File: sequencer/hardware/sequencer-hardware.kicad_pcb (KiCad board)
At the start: 4 copper layers, 54 parts, among them J10 Conn_01x03, J11 Conn_01x05_Male, J12 Conn_01x05_Male, J13 Conn_01x03, J14 Conn_01x03, J15 Conn_01x05_Male, J16 Conn_01x05_Male, J17 Conn_01x03, J2 40Pin 0.1", J3 USB_B_Micro, J4 Conn_01x02_Male, J7 Conn_01x03_Male, J8 Conn_01x03_Male, J9 Conn_01x03, U4 NCP1117-3.3_TO252, U6 W25Q128JVS, U7 RP2040, Y1 12MHz 18pF

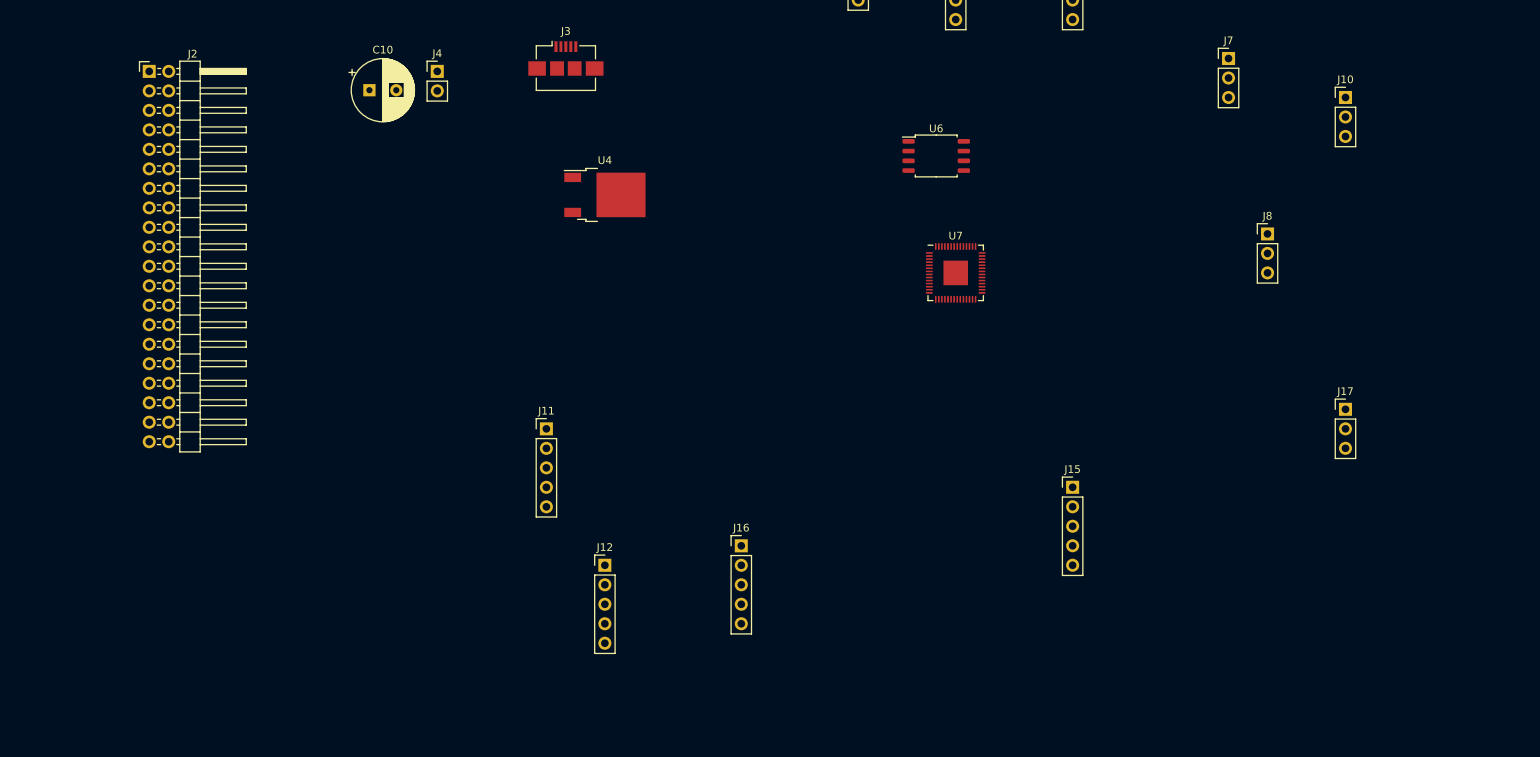
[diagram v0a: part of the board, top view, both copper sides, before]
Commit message: Disconnect GNDD from GNDA to prevent routing confusion
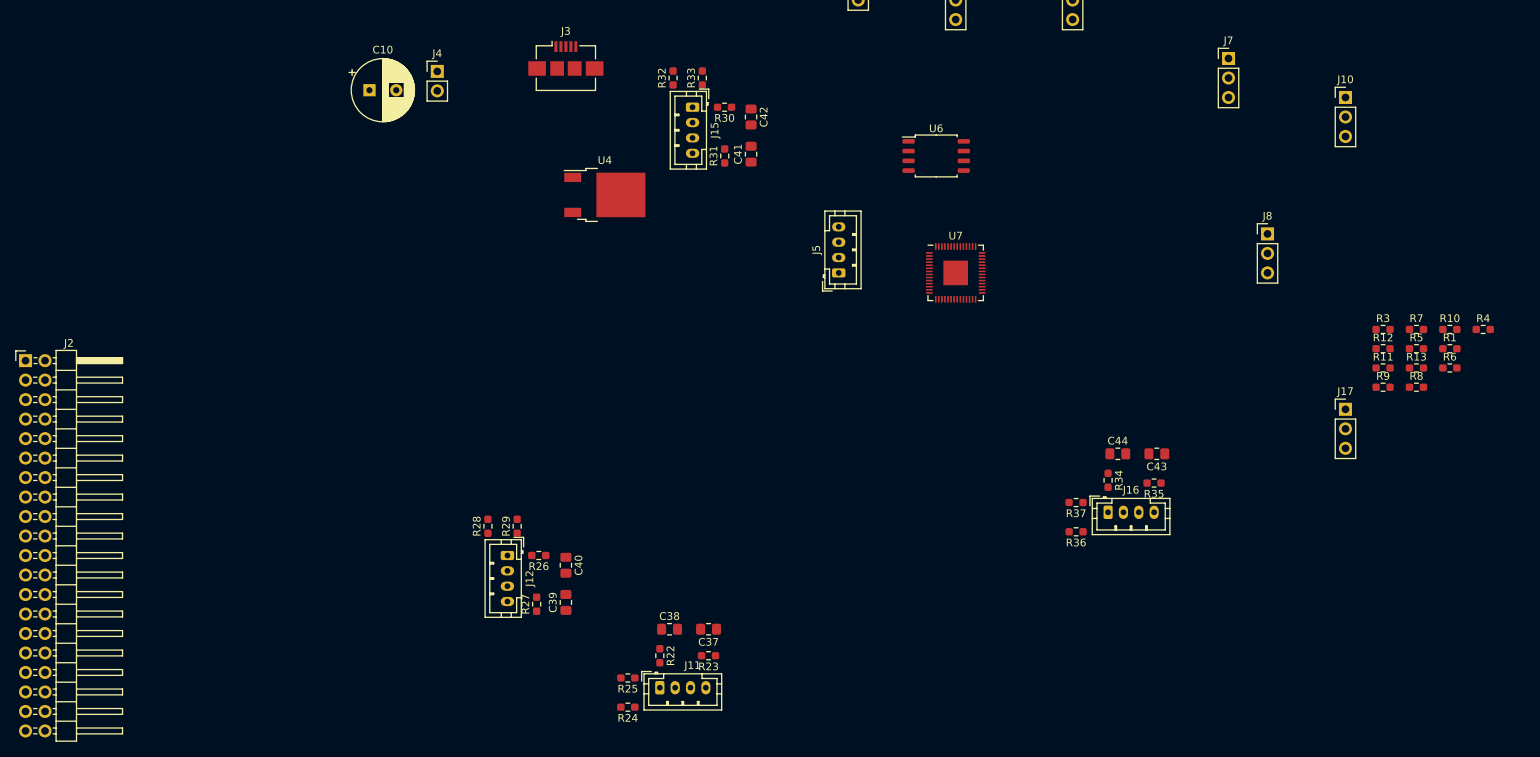
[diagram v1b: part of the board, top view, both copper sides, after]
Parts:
- added C37: 0.01u, Capacitor_SMD:C_0805_2012Metric_Pad1.18x1.45mm_HandSolder, F.Cu at (173.5, 130.3)
- added C38: 0.01u, Capacitor_SMD:C_0805_2012Metric_Pad1.18x1.45mm_HandSolder, F.Cu at (168.4, 130.3)
- added C39: 0.01u, Capacitor_SMD:C_0805_2012Metric_Pad1.18x1.45mm_HandSolder, F.Cu at (154.9, 126.8)
- added C40: 0.01u, Capacitor_SMD:C_0805_2012Metric_Pad1.18x1.45mm_HandSolder, F.Cu at (154.9, 121.9)
- added C41: 0.01u, Capacitor_SMD:C_0805_2012Metric_Pad1.18x1.45mm_HandSolder, F.Cu at (179.1, 68.3)
- added C42: 0.01u, Capacitor_SMD:C_0805_2012Metric_Pad1.18x1.45mm_HandSolder, F.Cu at (179.1, 63.5)
- added C43: 0.01u, Capacitor_SMD:C_0805_2012Metric_Pad1.18x1.45mm_HandSolder, F.Cu at (231.9, 107.4)
- added C44: 0.01u, Capacitor_SMD:C_0805_2012Metric_Pad1.18x1.45mm_HandSolder, F.Cu at (226.9, 107.4)
- added J5: JST 4-Pin male, Connector_JST:JST_PH_B4B-PH-K_1x04_P2.00mm_Vertical, F.Cu at (190.5, 83.8)
- added R1: 10k, Resistor_SMD:R_0603_1608Metric_Pad0.98x0.95mm_HandSolder, F.Cu at (270.1, 93.7)
- added R10: 10k, Resistor_SMD:R_0603_1608Metric_Pad0.98x0.95mm_HandSolder, F.Cu at (270.1, 91.2)
- added R11: 10k, Resistor_SMD:R_0603_1608Metric_Pad0.98x0.95mm_HandSolder, F.Cu at (261.4, 96.2)
- added R12: 10k, Resistor_SMD:R_0603_1608Metric_Pad0.98x0.95mm_HandSolder, F.Cu at (261.4, 93.7)
- added R13: 10k, Resistor_SMD:R_0603_1608Metric_Pad0.98x0.95mm_HandSolder, F.Cu at (265.8, 96.2)
- added R22: 10k, Resistor_SMD:R_0603_1608Metric_Pad0.98x0.95mm_HandSolder, F.Cu at (167.2, 133.7)
- added R23: 10k, Resistor_SMD:R_0603_1608Metric_Pad0.98x0.95mm_HandSolder, F.Cu at (173.5, 133.7)
- added R24: 10k, Resistor_SMD:R_0603_1608Metric_Pad0.98x0.95mm_HandSolder, F.Cu at (163.0, 140.4)
- added R25: 10k, Resistor_SMD:R_0603_1608Metric_Pad0.98x0.95mm_HandSolder, F.Cu at (163.0, 136.6)
- added R26: 10k, Resistor_SMD:R_0603_1608Metric_Pad0.98x0.95mm_HandSolder, F.Cu at (151.4, 120.7)
- added R27: 10k, Resistor_SMD:R_0603_1608Metric_Pad0.98x0.95mm_HandSolder, F.Cu at (151.1, 127.0)
- added R28: 10k, Resistor_SMD:R_0603_1608Metric_Pad0.98x0.95mm_HandSolder, F.Cu at (144.8, 116.8)
- added R29: 10k, Resistor_SMD:R_0603_1608Metric_Pad0.98x0.95mm_HandSolder, F.Cu at (148.6, 116.8)
- added R3: 10k, Resistor_SMD:R_0603_1608Metric_Pad0.98x0.95mm_HandSolder, F.Cu at (261.4, 91.2)
- added R30: 10k, Resistor_SMD:R_0603_1608Metric_Pad0.98x0.95mm_HandSolder, F.Cu at (175.6, 62.2)
- added R31: 10k, Resistor_SMD:R_0603_1608Metric_Pad0.98x0.95mm_HandSolder, F.Cu at (175.6, 68.6)
- added R32: 10k, Resistor_SMD:R_0603_1608Metric_Pad0.98x0.95mm_HandSolder, F.Cu at (168.9, 58.4)
- added R33: 10k, Resistor_SMD:R_0603_1608Metric_Pad0.98x0.95mm_HandSolder, F.Cu at (172.7, 58.4)
- added R34: 10k, Resistor_SMD:R_0603_1608Metric_Pad0.98x0.95mm_HandSolder, F.Cu at (225.6, 110.9)
- added R35: 10k, Resistor_SMD:R_0603_1608Metric_Pad0.98x0.95mm_HandSolder, F.Cu at (231.6, 111.2)
- added R36: 10k, Resistor_SMD:R_0603_1608Metric_Pad0.98x0.95mm_HandSolder, F.Cu at (221.4, 117.6)
- added R37: 10k, Resistor_SMD:R_0603_1608Metric_Pad0.98x0.95mm_HandSolder, F.Cu at (221.4, 113.8)
- added R4: 10k, Resistor_SMD:R_0603_1608Metric_Pad0.98x0.95mm_HandSolder, F.Cu at (274.5, 91.2)
- added R5: 10k, Resistor_SMD:R_0603_1608Metric_Pad0.98x0.95mm_HandSolder, F.Cu at (265.8, 93.7)
- added R6: 10k, Resistor_SMD:R_0603_1608Metric_Pad0.98x0.95mm_HandSolder, F.Cu at (270.1, 96.2)
- added R7: 10k, Resistor_SMD:R_0603_1608Metric_Pad0.98x0.95mm_HandSolder, F.Cu at (265.8, 91.2)
- added R8: 10k, Resistor_SMD:R_0603_1608Metric_Pad0.98x0.95mm_HandSolder, F.Cu at (265.8, 98.7)
- added R9: 10k, Resistor_SMD:R_0603_1608Metric_Pad0.98x0.95mm_HandSolder, F.Cu at (261.4, 98.7)
- J11, J12, J15, J16: value Conn_01x05_Male -> JST_4-pin_male; footprint Connector_PinHeader_2.54mm:PinHeader_1x05_P2.54mm_Vertical -> Connector_JST:JST_PH_B4B-PH-K_1x04_P2.00mm_Vertical
- moved J15 70.0 mm to (171.4, 62.2), turned to -90 degrees
- moved J16 48.0 mm to (225.6, 115.0)
- moved J2 41.0 mm to (84.5, 95.3)
- moved J11 36.8 mm to (167.2, 137.9)
- moved J12 12.8 mm to (147.3, 120.7), turned to -90 degrees
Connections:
- C10 pad 2: GNDA -> GNDD
- C11 pad 2: GNDA -> GNDD
- C20 pad 2: GNDA -> GNDD
- C21 pad 2: GNDA -> GNDD
- C22 pad 2: GNDA -> GNDD
- C23 pad 2: GNDA -> GNDD
- C24 pad 2: GNDA -> GNDD
- C25 pad 1: GNDA -> GNDD
- C26 pad 2: GNDA -> GNDD
- C27 pad 2: GNDA -> GNDD
- C28 pad 2: GNDA -> GNDD
- C29 pad 2: GNDA -> GNDD
- C30 pad 2: GNDA -> GNDD
- C31 pad 2: GNDA -> GNDD
- C32 pad 2: GNDA -> GNDD
- C33 pad 2: GNDA -> GNDD
- C34 pad 2: GNDA -> GNDD
- C35 pad 2: GNDA -> GNDD
- C36 pad 2: GNDA -> GNDD
- C9 pad 2: GNDA -> GNDD
- J10 pad 1: GNDA -> GNDD
- J11 pad 1: GNDA -> Net-(J11-Pad1)
- J11 pad 2: /D.R.U.M. Sequencer Digital/GPIO3_ENC02 -> GNDD
- J11 pad 3: /D.R.U.M. Sequencer Digital/GPIO2_ENC01 -> Net-(J11-Pad3)
- J11 pad 4: /D.R.U.M. Sequencer Digital/GPIO1_ENC00 -> unconnected-(J11-Pad4)
- J12 pad 1: GNDA -> Net-(J12-Pad1)
- J12 pad 2: /D.R.U.M. Sequencer Digital/GPIO11_ENC22 -> GNDD
- J12 pad 3: /D.R.U.M. Sequencer Digital/GPIO10_ENC21 -> Net-(J12-Pad3)
- J12 pad 4: /D.R.U.M. Sequencer Digital/GPIO9_ENC20 -> unconnected-(J12-Pad4)
- J13 pad 1: GNDA -> GNDD
- J14 pad 1: GNDA -> GNDD
- J15 pad 1: GNDA -> Net-(J15-Pad1)
- J15 pad 2: /D.R.U.M. Sequencer Digital/GPIO8_ENC12 -> GNDD
- J15 pad 3: /D.R.U.M. Sequencer Digital/GPIO7_ENC11 -> Net-(J15-Pad3)
- J15 pad 4: /D.R.U.M. Sequencer Digital/GPIO6_ENC10 -> unconnected-(J15-Pad4)
- J16 pad 1: GNDA -> Net-(J16-Pad1)
- J16 pad 2: /D.R.U.M. Sequencer Digital/GPIO14_ENC32 -> GNDD
- J16 pad 3: /D.R.U.M. Sequencer Digital/GPIO13_ENC31 -> Net-(J16-Pad3)
- J16 pad 4: /D.R.U.M. Sequencer Digital/GPIO12_ENC30 -> unconnected-(J16-Pad4)
- J17 pad 2: GNDA -> GNDD
- J2 pad 22: GNDA -> GNDD
- J2 pad 23: GNDA -> GNDD
- J2 pad 26: GNDA -> GNDD
- J2 pad 27: GNDA -> GNDD
- J2 pad 30: GNDA -> GNDD
- J2 pad 31: GNDA -> GNDD
- J2 pad 34: GNDA -> GNDD
- J2 pad 35: GNDA -> GNDD
- J2 pad 38: GNDA -> GNDD
- J2 pad 39: GNDA -> GNDD
- J3 pad 5: GNDA -> GNDD
- J3 pad 6: GNDA -> GNDD
- J7 pad 1: GNDA -> GNDD
- J8 pad 1: GNDA -> GNDD
- J9 pad 1: GNDA -> GNDD
- U4 pad 1: GNDA -> GNDD
- U6 pad 4: GNDA -> GNDD
- U7 pad 11: /D.R.U.M. Sequencer Digital/GPIO8_ENC12 -> unconnected-(U7-Pad11)
- U7 pad 14: /D.R.U.M. Sequencer Digital/GPIO11_ENC22 -> unconnected-(U7-Pad14)
- U7 pad 17: /D.R.U.M. Sequencer Digital/GPIO14_ENC32 -> unconnected-(U7-Pad17)
- U7 pad 19: GNDA -> GNDD
- U7 pad 5: /D.R.U.M. Sequencer Digital/GPIO3_ENC02 -> unconnected-(U7-Pad5)
- U7 pad 57: GNDA -> GNDD

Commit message: Do a lot of random stuff
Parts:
- added SW2: SW_Push, custom:TE_ConnMSLPT5252CG1, F.Cu at (212.1, 135.9)
- added SW3: SW_Push, custom:TE_ConnMSLPT5252CG1, F.Cu at (228.8, 135.9)
- added U5: OPA703UA, Package_SO:SOIC-8_3.9x4.9mm_P1.27mm, F.Cu at (59.9, 78.6)
- C21, C23, C29: value 1u -> 0.01u; footprint Capacitor_SMD:C_0603_1608Metric_Pad1.08x0.95mm_HandSolder -> Capacitor_SMD:C_0805_2012Metric_Pad1.18x1.45mm_HandSolder
- C24: value 0.1u -> 1u
- C25: value 27p -> 0.01u; footprint Capacitor_SMD:C_0603_1608Metric_Pad1.08x0.95mm_HandSolder -> Capacitor_SMD:C_0805_2012Metric_Pad1.18x1.45mm_HandSolder
- C26: value 27p -> 1u
- C27, C28, C30, C31: value 0.1u -> 0.01u; footprint Capacitor_SMD:C_0603_1608Metric_Pad1.08x0.95mm_HandSolder -> Capacitor_SMD:C_0805_2012Metric_Pad1.18x1.45mm_HandSolder
- C33, C34: value 0.1u -> 27p
- C36: value 1u -> 0.1u
- C37, C44: value 0.01u -> 1u; footprint Capacitor_SMD:C_0805_2012Metric_Pad1.18x1.45mm_HandSolder -> Capacitor_SMD:C_0603_1608Metric_Pad1.08x0.95mm_HandSolder
- C38, C39, C40, C41, C42, C43: value 0.01u -> 0.1u; footprint Capacitor_SMD:C_0805_2012Metric_Pad1.18x1.45mm_HandSolder -> Capacitor_SMD:C_0603_1608Metric_Pad1.08x0.95mm_HandSolder
- J10, J9: value Conn_01x03 -> JST_4-pin_male; footprint Connector_PinHeader_2.54mm:PinHeader_1x03_P2.54mm_Vertical -> Connector_JST:JST_PH_B4B-PH-K_1x04_P2.00mm_Vertical
- J11, J12: value JST_4-pin_male -> Conn_01x03; footprint Connector_JST:JST_PH_B4B-PH-K_1x04_P2.00mm_Vertical -> Connector_PinHeader_2.54mm:PinHeader_1x03_P2.54mm_Vertical
- R18, R21: value 1k -> 10k
- R19, R20: value 27 -> 10k
- R26, R37: value 10k -> 1k
- R35, R36: value 10k -> 27
- U6: value W25Q128JVS -> OPA703UA; footprint Package_SO:SOIC-8_5.23x5.23mm_P1.27mm -> Package_SO:SOIC-8_3.9x4.9mm_P1.27mm
- U7: value RP2040 -> W25Q128JVS; footprint Package_DFN_QFN:QFN-56-1EP_7x7mm_P0.4mm_EP3.2x3.2mm -> Package_SO:SOIC-8_5.23x5.23mm_P1.27mm
- moved R13 217.6 mm to (48.8, 80.9), turned to 180 degrees
- moved R4 209.8 mm to (65.5, 72.9), turned to 180 degrees
- moved R12 207.7 mm to (54.4, 78.0), turned to 180 degrees
- moved R6 205.4 mm to (65.5, 78.0), turned to 180 degrees
- moved R10 204.6 mm to (65.5, 88.1), turned to 180 degrees
- moved R11 202.1 mm to (59.8, 82.0), turned to 180 degrees
- moved R5 201.1 mm to (65.5, 75.4), turned to 180 degrees
- moved R8 200.9 mm to (65.5, 83.1), turned to 180 degrees
- moved R7 200.5 mm to (65.5, 80.5), turned to 180 degrees
- moved R3 197.0 mm to (65.5, 70.4), turned to 180 degrees
- moved R9 196.3 mm to (65.5, 85.6), turned to 180 degrees
- moved U6 154.7 mm to (48.8, 77.3), turned to 180 degrees
- moved C19 126.4 mm to (70.6, 88.1), turned to 180 degrees
- moved C18 118.6 mm to (70.6, 83.1)
- moved J10 117.6 mm to (167.6, 137.9)
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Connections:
- C21 pad 1: +3V3 -> /D.R.U.M. Sequencer Digital/GPIO2_ENC01
- C23 pad 1: +3V3 -> /D.R.U.M. Sequencer Digital/GPIO1_ENC00
- C25 pad 1: GNDD -> /D.R.U.M. Sequencer Digital/GPIO10_ENC21
- C25 pad 2: Net-(C25-Pad2) -> GNDD
- C26 pad 1: Net-(C26-Pad1) -> +3V3
- C27 pad 1: +1V1 -> /D.R.U.M. Sequencer Digital/GPIO9_ENC20
- C28 pad 1: +1V1 -> /D.R.U.M. Sequencer Digital/GPIO7_ENC11
- C29 pad 1: +1V1 -> /D.R.U.M. Sequencer Digital/GPIO6_ENC10
- C30 pad 1: +3V3 -> /D.R.U.M. Sequencer Digital/GPIO13_ENC31
- C31 pad 1: +3V3 -> /D.R.U.M. Sequencer Digital/GPIO12_ENC30
- C33 pad 1: +3V3 -> GNDD
- C33 pad 2: GNDD -> Net-(C33-Pad2)
- C34 pad 1: +3V3 -> Net-(C34-Pad1)
- C35 pad 1: +3V3 -> +1V1
- C36 pad 1: +3V3 -> +1V1
- C37 pad 1: /D.R.U.M. Sequencer Digital/GPIO2_ENC01 -> +1V1
- C38 pad 1: /D.R.U.M. Sequencer Digital/GPIO1_ENC00 -> +3V3
- C39 pad 1: /D.R.U.M. Sequencer Digital/GPIO10_ENC21 -> +3V3
- C40 pad 1: /D.R.U.M. Sequencer Digital/GPIO9_ENC20 -> +3V3
- C41 pad 1: /D.R.U.M. Sequencer Digital/GPIO7_ENC11 -> +3V3
- C42 pad 1: /D.R.U.M. Sequencer Digital/GPIO6_ENC10 -> +3V3
- C43 pad 1: /D.R.U.M. Sequencer Digital/GPIO13_ENC31 -> +3V3
- C44 pad 1: /D.R.U.M. Sequencer Digital/GPIO12_ENC30 -> +3V3
- J10 pad 1: GNDD -> Net-(J10-Pad1)
- J10 pad 2: /D.R.U.M. Sequencer Digital/GPIO28_ADC2 -> GNDD
- J10 pad 3: +3V3 -> Net-(J10-Pad3)
- J11 pad 1: Net-(J11-Pad1) -> GNDD
- J11 pad 2: GNDD -> /D.R.U.M. Sequencer Digital/GPIO26_ADC0
- J11 pad 3: Net-(J11-Pad3) -> +3V3
- J12 pad 1: Net-(J12-Pad1) -> GNDD
- J12 pad 2: GNDD -> /D.R.U.M. Sequencer Digital/GPIO28_ADC2
- J12 pad 3: Net-(J12-Pad3) -> +3V3
- J9 pad 1: GNDD -> Net-(J9-Pad1)
- J9 pad 2: /D.R.U.M. Sequencer Digital/GPIO26_ADC0 -> GNDD
- J9 pad 3: +3V3 -> Net-(J9-Pad3)
- R17 pad 1: +3V3 -> /D.R.U.M. Sequencer Digital/GPIO1_ENC00
- R17 pad 2: /D.R.U.M. Sequencer Digital/FCSB -> Net-(J9-Pad1)
- R18 pad 1: /D.R.U.M. Sequencer Digital/FCSB -> /D.R.U.M. Sequencer Digital/GPIO2_ENC01
- R18 pad 2: Net-(R18-Pad2) -> Net-(J9-Pad3)
- R19 pad 1: /USB_D+ -> Net-(J9-Pad3)
- R19 pad 2: /D.R.U.M. Sequencer Digital/_USB_D+ -> +3V3
- R20 pad 1: /USB_D- -> Net-(J9-Pad1)
- R20 pad 2: /D.R.U.M. Sequencer Digital/_USB_D- -> +3V3
- R21 pad 1: Net-(C26-Pad1) -> /D.R.U.M. Sequencer Digital/GPIO9_ENC20
- R21 pad 2: Net-(R21-Pad2) -> Net-(J10-Pad1)
- R22 pad 1: /D.R.U.M. Sequencer Digital/GPIO1_ENC00 -> /D.R.U.M. Sequencer Digital/GPIO10_ENC21
- R22 pad 2: Net-(J11-Pad1) -> Net-(J10-Pad3)
- R23 pad 1: /D.R.U.M. Sequencer Digital/GPIO2_ENC01 -> Net-(J10-Pad3)
- R23 pad 2: Net-(J11-Pad3) -> +3V3
- R24 pad 1: Net-(J11-Pad3) -> Net-(J10-Pad1)
- R25 pad 1: Net-(J11-Pad1) -> +3V3
- R25 pad 2: +3V3 -> /D.R.U.M. Sequencer Digital/FCSB
- R26 pad 1: /D.R.U.M. Sequencer Digital/GPIO9_ENC20 -> /D.R.U.M. Sequencer Digital/FCSB
- R26 pad 2: Net-(J12-Pad1) -> Net-(R26-Pad2)
- R27 pad 1: /D.R.U.M. Sequencer Digital/GPIO10_ENC21 -> /D.R.U.M. Sequencer Digital/GPIO6_ENC10
- R27 pad 2: Net-(J12-Pad3) -> Net-(J15-Pad1)
- R28 pad 1: Net-(J12-Pad3) -> /D.R.U.M. Sequencer Digital/GPIO7_ENC11
- R28 pad 2: +3V3 -> Net-(J15-Pad3)
- R29 pad 1: Net-(J12-Pad1) -> Net-(J15-Pad3)
- R30 pad 1: /D.R.U.M. Sequencer Digital/GPIO6_ENC10 -> Net-(J15-Pad1)
- R30 pad 2: Net-(J15-Pad1) -> +3V3
- R31 pad 1: /D.R.U.M. Sequencer Digital/GPIO7_ENC11 -> /D.R.U.M. Sequencer Digital/GPIO12_ENC30
- R31 pad 2: Net-(J15-Pad3) -> Net-(J16-Pad1)
- R32 pad 1: Net-(J15-Pad3) -> /D.R.U.M. Sequencer Digital/GPIO13_ENC31
- R32 pad 2: +3V3 -> Net-(J16-Pad3)
- R33 pad 1: Net-(J15-Pad1) -> Net-(J16-Pad3)
- R34 pad 1: /D.R.U.M. Sequencer Digital/GPIO12_ENC30 -> Net-(J16-Pad1)
- R34 pad 2: Net-(J16-Pad1) -> +3V3
- R35 pad 1: /D.R.U.M. Sequencer Digital/GPIO13_ENC31 -> /USB_D+
- R35 pad 2: Net-(J16-Pad3) -> /D.R.U.M. Sequencer Digital/_USB_D+
- R36 pad 1: Net-(J16-Pad3) -> /USB_D-
- R36 pad 2: +3V3 -> /D.R.U.M. Sequencer Digital/_USB_D-
- R37 pad 1: Net-(J16-Pad1) -> Net-(C34-Pad1)
- R37 pad 2: +3V3 -> Net-(R37-Pad2)
- U6 pad 1: /D.R.U.M. Sequencer Digital/FCSB -> (no net)
- U6 pad 2: /D.R.U.M. Sequencer Digital/FD1 -> Net-(R12-Pad2)
- U6 pad 3: /D.R.U.M. Sequencer Digital/FD2 -> GNDA
- U6 pad 4: GNDD -> +5VA
- U6 pad 5: /D.R.U.M. Sequencer Digital/FD0 -> (no net)
- U6 pad 6: /D.R.U.M. Sequencer Digital/FSCLK -> Net-(R14-Pad1)
- U6 pad 7: /D.R.U.M. Sequencer Digital/FD3 -> -5V
- U6 pad 8: +3V3 -> (no net)
- U7 pad 1: +3V3 -> /D.R.U.M. Sequencer Digital/FCSB
- U7 pad 2: unconnected-(U7-Pad2) -> /D.R.U.M. Sequencer Digital/FD1
- U7 pad 3: /D.R.U.M. Sequencer Digital/GPIO1_ENC00 -> /D.R.U.M. Sequencer Digital/FD2
- U7 pad 4: /D.R.U.M. Sequencer Digital/GPIO2_ENC01 -> GNDD
- U7 pad 5: unconnected-(U7-Pad5) -> /D.R.U.M. Sequencer Digital/FD0
- U7 pad 6: /KEY_SDA -> /D.R.U.M. Sequencer Digital/FSCLK
- U7 pad 7: /KEY_SCL -> /D.R.U.M. Sequencer Digital/FD3
- U7 pad 8: /D.R.U.M. Sequencer Digital/GPIO6_ENC10 -> +3V3
- Y1 pad 1: Net-(C25-Pad2) -> Net-(C33-Pad2)
- Y1 pad 2: Net-(C26-Pad1) -> Net-(C34-Pad1)

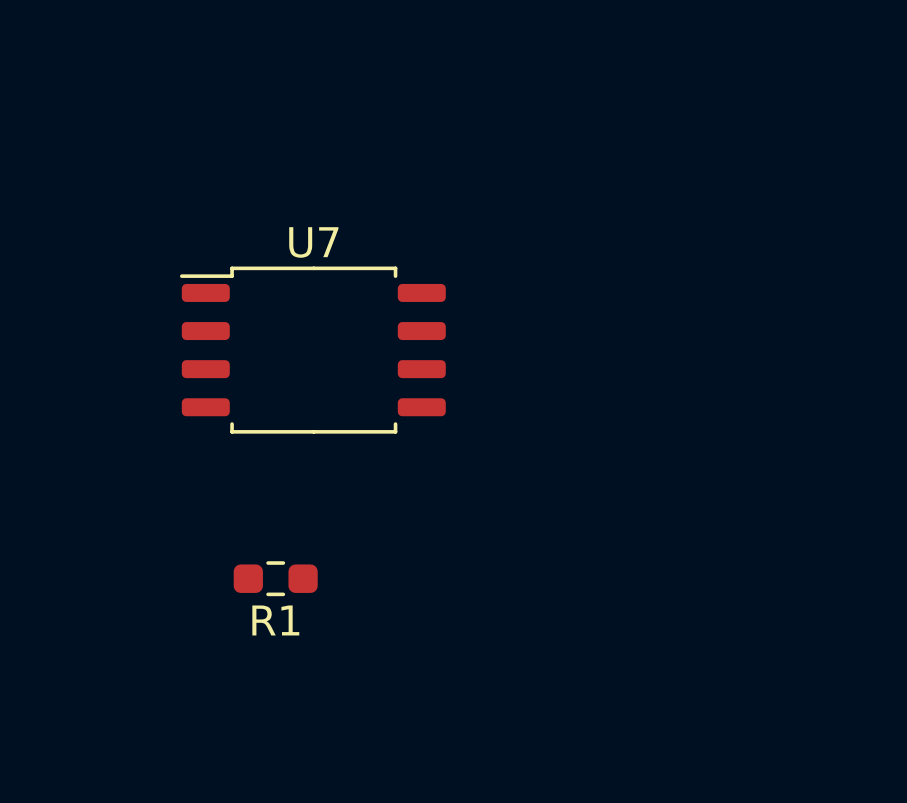
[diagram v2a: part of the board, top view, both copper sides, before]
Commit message: Add project copy of RP2040 footprint
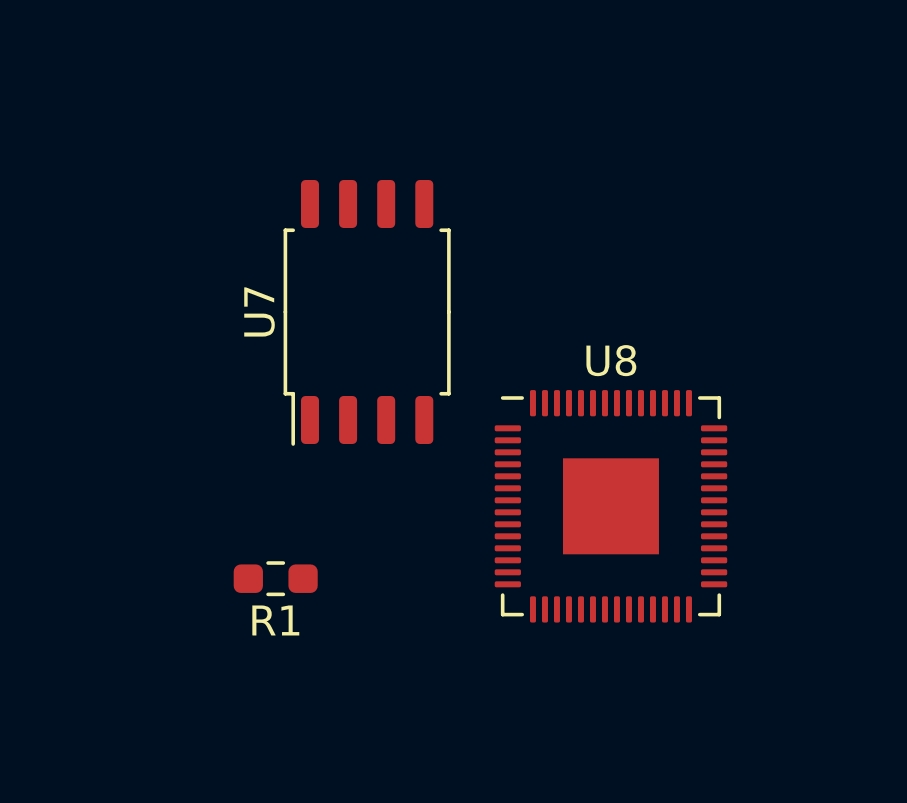
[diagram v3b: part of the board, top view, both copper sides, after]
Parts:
- added U8: RP2040, Package_DFN_QFN:QFN-56-1EP_7x7mm_P0.4mm_EP3.2x3.2mm, F.Cu at (215.6, 89.0)
- moved U7 2.18 mm to (207.5, 82.5), turned to 90 degrees

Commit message: more library weirdness
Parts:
- moved U8 13.7 mm to (229.3, 87.8)
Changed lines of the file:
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@@
   )
   (footprint "Package_DFN_QFN:QFN-56-1EP_7x7mm_P0.4mm_EP3.2x3.2mm" (layer "F.Cu")
-    (at 215.646 89.027)
+    (at 229.324 87.846)
     (descr "QFN, 56 Pin (https://datasheets.raspberrypi.com/rp2040/rp2040-datasheet.pdf#page=634), generated with kicad-footprint-generator ipc_noLead_generator.py")
     (tags "QFN NoLead")

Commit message: some routing added
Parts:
- added C1: 10uF, Capacitor_SMD:C_1206_3216Metric_Pad1.33x1.80mm_HandSolder, F.Cu at (18.1, 135.9)
- added C2: 100uF, Capacitor_THT:CP_Radial_D8.0mm_P3.50mm, F.Cu at (25.4, 135.9)
- added C3: 10uF, Capacitor_SMD:C_1206_3216Metric_Pad1.33x1.80mm_HandSolder, F.Cu at (43.2, 17.8)
- added C4: 100uF, Capacitor_THT:CP_Radial_D8.0mm_P3.50mm, F.Cu at (30.5, 22.9)
- added C5: 10uF, Capacitor_SMD:C_1206_3216Metric_Pad1.33x1.80mm_HandSolder, F.Cu at (22.9, 20.3)
- added C6: 10uF, Capacitor_SMD:C_1206_3216Metric_Pad1.33x1.80mm_HandSolder, F.Cu at (61.0, 152.4)
- added C7: 100uF, Capacitor_THT:CP_Radial_D8.0mm_P3.50mm, F.Cu at (63.5, 158.8)
- added C8: 10uF, Capacitor_SMD:C_1206_3216Metric_Pad1.33x1.80mm_HandSolder, F.Cu at (40.6, 45.7)
- added FL1: Choke, Inductor_THT:Choke_Schaffner_RN102-04-14.0x14.0mm, F.Cu at (26.7, 120.9)
- added J1: Barrel Jack, Connector_BarrelJack:BarrelJack_Horizontal, F.Cu at (23.8, 111.5)
- added J6: TS Out, Connector_Audio:Jack_6.35mm_Neutrik_NRJ6HF-AU_Horizontal, F.Cu at (69.5, 22.2)
- added R14: 200, Resistor_SMD:R_0603_1608Metric_Pad0.98x0.95mm_HandSolder, F.Cu at (43.2, 78.7)
- added RV1: 1k Audio Taper Pot, custom:LINPOT-10KDB, F.Cu at (27.9, 116.8)
- added U1: L7805_A, Package_TO_SOT_THT:TO-220-3_Horizontal_TabDown, F.Cu at (73.7, 62.6)
- added U2: L7805_D, Package_TO_SOT_THT:TO-220-3_Horizontal_TabDown, F.Cu at (58.4, 162.6)
- added U3: ICL7660, Package_SO:SOIC-8_3.9x4.9mm_P1.27mm, F.Cu at (27.9, 48.3)
- U8: footprint Package_DFN_QFN:QFN-56-1EP_7x7mm_P0.4mm_EP3.2x3.2mm -> custom:QFN-56-1EP_7x7mm_P0.4mm_EP3.2x3.2mm
- moved C11 135.6 mm to (61.0, 147.3), turned to -90 degrees
- moved C9 134.5 mm to (63.5, 152.8), turned to 90 degrees
- moved U4 127.9 mm to (56.1, 148.2), turned to 90 degrees
- moved C10 107.6 mm to (64.8, 146.1)
